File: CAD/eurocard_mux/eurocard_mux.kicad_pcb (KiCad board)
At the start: 2 copper layers, 124 x 60 mm, 20 parts, among them J1 1759091, J2 1759091, J3 MC-254-12-00-RA-DIP, J4 MC-254-12-00-RA-DIP, J5 1759091, K1 AGQ210A12Z, K2 AGQ210A12Z, K3 AGQ210A12Z, K4 AGQ210A12Z, K5 AGQ210A12Z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

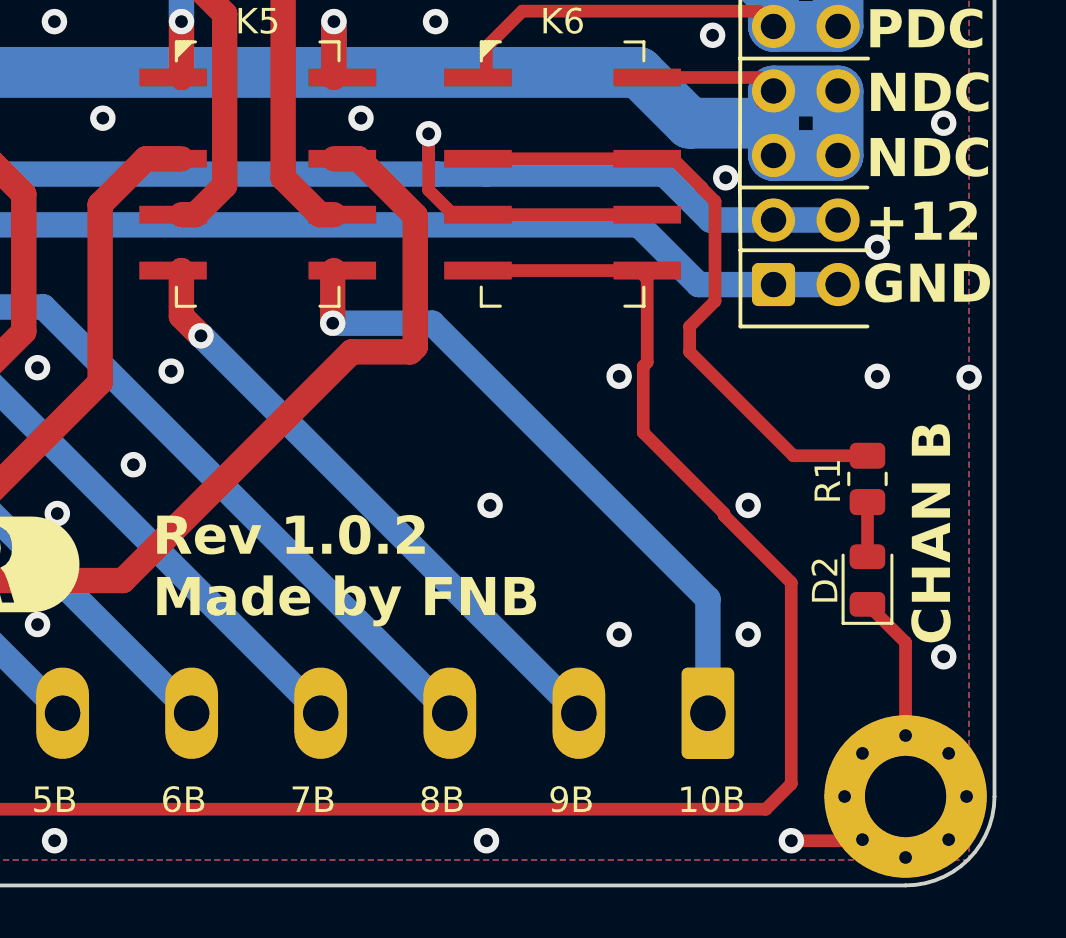
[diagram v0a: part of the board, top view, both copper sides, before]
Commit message: Switched let connections for correct id
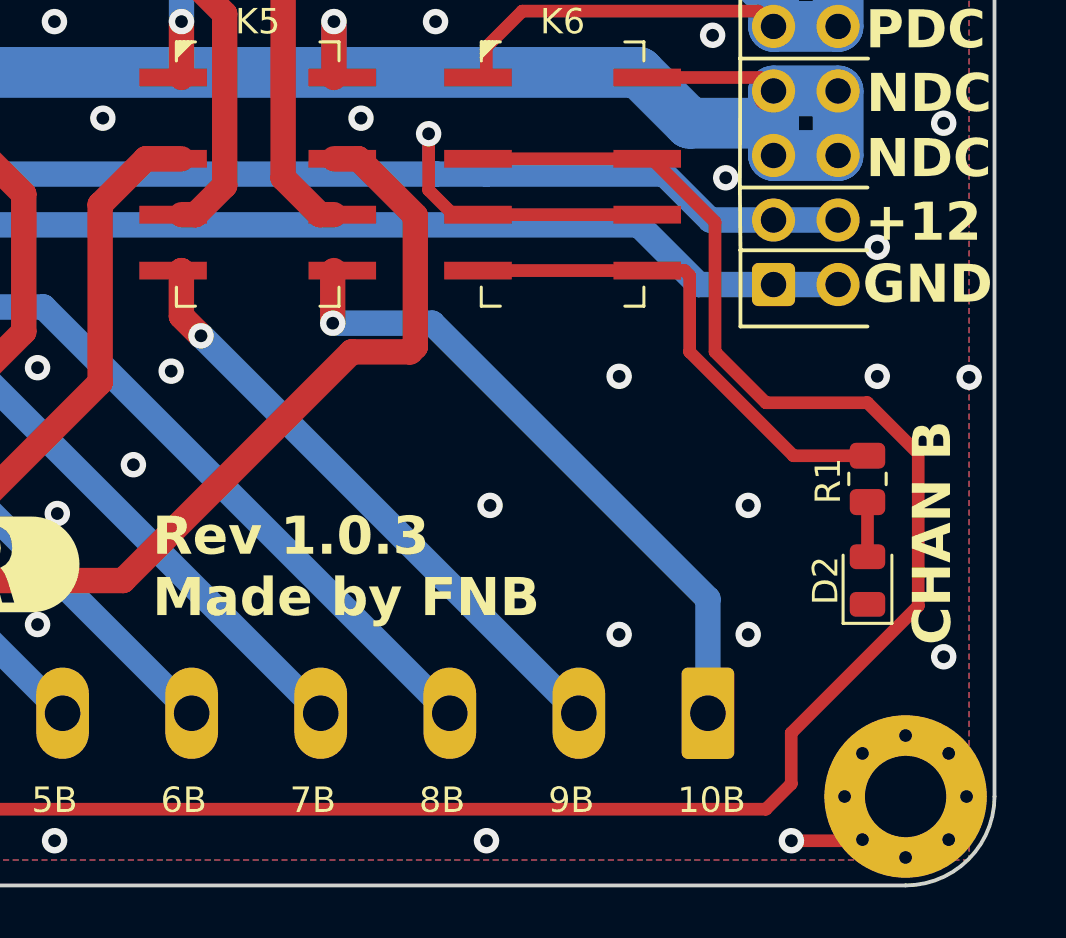
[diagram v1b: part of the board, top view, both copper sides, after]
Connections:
- R1 pad 1: /CHNA -> /CHNB
- R2 pad 1: /CHNB -> /CHNA
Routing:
- net /CHNA: track 24.7 -> 161.7 mm
- net /CHNB: track 150.6 -> 19.8 mm
- net GND: track 161.2 -> 153.0 mm
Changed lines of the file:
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@@
 		(title "Mina ERT multiplexer")
 		(date "2025-12-09")
-		(rev "1.0.2")
+		(rev "1.0.3")
 		(company "Made By FNB")
 	)
@@
 		(property ki_fp_filters "Relay*DPDT*Kemet*EE2*NU*")
 		(sheetname "/")
-		(sheetfile "eurocard mux.kicad_sch")
+		(sheetfile "eurocard_mux.kicad_sch")
 		(attr smd)
 		(fp_line
@@
 		(property ki_fp_filters "Relay*DPDT*Kemet*EE2*NU*")
 		(sheetname "/")
-		(sheetfile "eurocard mux.kicad_sch")
+		(sheetfile "eurocard_mux.kicad_sch")
 		(attr smd)
 		(fp_line
@@
 		(property ki_fp_filters "Relay*DPDT*Kemet*EE2*NU*")
 		(sheetname "/")
-		(sheetfile "eurocard mux.kicad_sch")
+		(sheetfile "eurocard_mux.kicad_sch")
 		(attr smd)
 		(fp_line
@@
 		(property ki_fp_filters "R_*")
 		(sheetname "/")
-		(sheetfile "eurocard mux.kicad_sch")
+		(sheetfile "eurocard_mux.kicad_sch")
 		(attr smd)
 		(fp_line
@@
 			(layers "F.Cu" "F.Mask" "F.Paste")
 			(roundrect_rratio 0.243902)
-			(net 37 "/CHNB")
+			(net 38 "/CHNA")
 			(pintype "passive")
 		)
@@
 		(property ki_fp_filters "Connector*:*_2x??_*")
 		(sheetname "/")
-		(sheetfile "eurocard mux.kicad_sch")
+		(sheetfile "eurocard_mux.kicad_sch")
 		(attr through_hole)
 		(fp_line
@@
 		(property ki_fp_filters "MountingHole*Pad*")
 		(sheetname "/")
-		(sheetfile "eurocard mux.kicad_sch")
+		(sheetfile "eurocard_mux.kicad_sch")
 		(attr exclude_from_pos_files exclude_from_bom)
 		(fp_circle
@@
 		(property ki_fp_filters "LED* LED_SMD:* LED_THT:*")
 		(sheetname "/")
-		(sheetfile "eurocard mux.kicad_sch")
+		(sheetfile "eurocard_mux.kicad_sch")
 		(attr smd)
 		(fp_line
@@
 		(property ki_fp_filters "Relay*DPDT*Kemet*EE2*NU*")
 		(sheetname "/")
-		(sheetfile "eurocard mux.kicad_sch")
+		(sheetfile "eurocard_mux.kicad_sch")
 		(attr smd)
 		(fp_line
@@
 		(property ki_fp_filters "Connector*:*_1x??_*")
 		(sheetname "/")
-		(sheetfile "eurocard mux.kicad_sch")
+		(sheetfile "eurocard_mux.kicad_sch")
 		(attr through_hole)
 		(fp_line
@@
 		(property ki_fp_filters "MountingHole*Pad*")
 		(sheetname "/")
-		(sheetfile "eurocard mux.kicad_sch")
+		(sheetfile "eurocard_mux.kicad_sch")
 		(attr exclude_from_pos_files exclude_from_bom)
 		(fp_circle
@@
 		(property ki_fp_filters "R_*")
 		(sheetname "/")
-		(sheetfile "eurocard mux.kicad_sch")
+		(sheetfile "eurocard_mux.kicad_sch")
 		(attr smd)
 		(fp_line
@@
 			(layers "F.Cu" "F.Mask" "F.Paste")
 			(roundrect_rratio 0.243902)
-			(net 38 "/CHNA")
+			(net 37 "/CHNB")
 			(pintype "passive")
 		)
@@
 		(property ki_fp_filters "MountingHole*Pad*")
 		(sheetname "/")
-		(sheetfile "eurocard mux.kicad_sch")
+		(sheetfile "eurocard_mux.kicad_sch")
 		(attr exclude_from_pos_files exclude_from_bom)
 		(fp_circle
@@
 		(property ki_fp_filters "Relay*DPDT*Kemet*EE2*NU*")
 		(sheetname "/")
-		(sheetfile "eurocard mux.kicad_sch")
+		(sheetfile "eurocard_mux.kicad_sch")
 		(attr smd)
 		(fp_line
@@
 		(property ki_fp_filters "MountingHole*Pad*")
 		(sheetname "/")
-		(sheetfile "eurocard mux.kicad_sch")
+		(sheetfile "eurocard_mux.kicad_sch")
 		(attr exclude_from_pos_files exclude_from_bom)
 		(fp_circle
@@
 		(property ki_fp_filters "LED* LED_SMD:* LED_THT:*")
 		(sheetname "/")
-		(sheetfile "eurocard mux.kicad_sch")
+		(sheetfile "eurocard_mux.kicad_sch")
 		(attr smd)
 		(fp_line
@@
 		(property ki_fp_filters "Relay*DPDT*Kemet*EE2*NU*")
 		(sheetname "/")
-		(sheetfile "eurocard mux.kicad_sch")
+		(sheetfile "eurocard_mux.kicad_sch")
 		(attr smd)
 		(fp_line
@@
 		(property ki_fp_filters "Connector*:*_2x??_*")
 		(sheetname "/")
-		(sheetfile "eurocard mux.kicad_sch")
+		(sheetfile "eurocard_mux.kicad_sch")
 		(attr through_hole)
 		(fp_line
@@
 		(property ki_fp_filters "Connector*:*_1x??_*")
 		(sheetname "/")
-		(sheetfile "eurocard mux.kicad_sch")
+		(sheetfile "eurocard_mux.kicad_sch")
 		(attr through_hole)
 		(fp_line
@@
 		(property ki_fp_filters "Connector*:*_1x??_*")
 		(sheetname "/")
-		(sheetfile "eurocard mux.kicad_sch")
+		(sheetfile "eurocard_mux.kicad_sch")
 		(attr through_hole)
 		(fp_line
@@
 	)
 	(segment
-		(start 175.5 141.5)
-		(end 175.5 135.4375)
-		(width 0.5)
-		(layer "F.Cu")
-		(net 33)
-	)
-	(segment
 		(start 62.5 141.5)
 		(end 64 143)
@@
 	)
 	(segment
-		(start 175.5 135.4375)
-		(end 174 133.9375)
-		(width 0.5)
-		(layer "F.Cu")
-		(net 33)
-	)
-	(segment
 		(start 58.5 88.5)
 		(end 58.5 93.527227)
@@
 	)
 	(segment
-		(start 165.329222 124.415087)
-		(end 165.176477 124.567832)
-		(width 0.5)
-		(layer "F.Cu")
-		(net 37)
-	)
-	(segment
-		(start 165.176477 127.176477)
-		(end 168.354477 130.354477)
-		(width 0.5)
-		(layer "F.Cu")
-		(net 37)
-	)
-	(segment
-		(start 61.85 129.15)
-		(end 63 129.15)
-		(width 0.5)
-		(layer "F.Cu")
-		(net 37)
-	)
-	(segment
-		(start 168.354477 130.435668)
-		(end 171 133.081191)
+		(start 167 121)
+		(end 167 124)
 		(width 0.5)
 		(layer "F.Cu")
@@
 	)
 	(segment
-		(start 171 141)
-		(end 170 142)
+		(start 165 120.8)
+		(end 166.8 120.8)
 		(width 0.5)
 		(layer "F.Cu")
@@
 	)
 	(segment
-		(start 165 120.8)
-		(end 165.329222 121.129222)
+		(start 166.8 120.8)
+		(end 167 121)
 		(width 0.5)
 		(layer "F.Cu")
@@
 	)
 	(segment
-		(start 165.329222 121.129222)
-		(end 165.329222 124.415087)
+		(start 171.0875 128.0875)
+		(end 174 128.0875)
 		(width 0.5)
 		(layer "F.Cu")
@@
 	)
 	(segment
-		(start 165.176477 124.567832)
-		(end 165.176477 127.176477)
+		(start 167 124)
+		(end 171.0875 128.0875)
 		(width 0.5)
 		(layer "F.Cu")
@@
 	)
 	(segment
-		(start 61 137)
-		(end 61 130)
+		(start 174 126)
+		(end 176 128)
 		(width 0.5)
 		(layer "F.Cu")
-		(net 37)
+		(net 38)
 	)
 	(segment
-		(start 66 142)
-		(end 61 137)
+		(start 61 130)
+		(end 61.85 129.15)
 		(width 0.5)
 		(layer "F.Cu")
-		(net 37)
+		(net 38)
 	)
 	(segment
-		(start 168.354477 130.354477)
-		(end 168.354477 130.435668)
+		(start 159 116.4)
+		(end 165 116.4)
 		(width 0.5)
 		(layer "F.Cu")
-		(net 37)
+		(net 38)
 	)
 	(segment
-		(start 61 130)
-		(end 61.85 129.15)
+		(start 168 124)
+		(end 170 126)
 		(width 0.5)
 		(layer "F.Cu")
-		(net 37)
+		(net 38)
 	)
 	(segment
-		(start 170 142)
-		(end 66 142)
+		(start 170 126)
+		(end 174 126)
 		(width 0.5)
 		(layer "F.Cu")
-		(net 37)
+		(net 38)
 	)
 	(segment
-		(start 171 133.081191)
-		(end 171 141)
+		(start 171 141)
+		(end 170 142)
 		(width 0.5)
 		(layer "F.Cu")
-		(net 37)
+		(net 38)
 	)
 	(segment
-		(start 171.0875 128.0875)
-		(end 167 124)
+		(start 176 134)
+		(end 171 139)
 		(width 0.5)
 		(layer "F.Cu")
@@
 	)
 	(segment
-		(start 159 116.4)
-		(end 165 116.4)
+		(start 66 142)
+		(end 61 137)
 		(width 0.5)
 		(layer "F.Cu")
@@
 	)
 	(segment
-		(start 166.349684 116.4)
-		(end 165 116.4)
+		(start 165.511 116.4)
+		(end 168 118.889)
 		(width 0.5)
 		(layer "F.Cu")
@@
 	)
 	(segment
-		(start 167.469104 117.51942)
-		(end 166.349684 116.4)
+		(start 168 118.889)
+		(end 168 124)
 		(width 0.5)
 		(layer "F.Cu")
@@
 	)
 	(segment
-		(start 167 124)
-		(end 167 123)
+		(start 61 137)
+		(end 61 130)
 		(width 0.5)
 		(layer "F.Cu")
@@
 	)
 	(segment
-		(start 174 128.0875)
-		(end 171.0875 128.0875)
+		(start 171 139)
+		(end 171 141)
 		(width 0.5)
 		(layer "F.Cu")
@@
 	)
 	(segment
-		(start 168 122)
-		(end 168 118.072271)
+		(start 61.85 129.15)
+		(end 63 129.15)
 		(width 0.5)
 		(layer "F.Cu")
@@
 	)
 	(segment
-		(start 168 118.072271)
-		(end 167.469104 117.541375)
+		(start 170 142)
+		(end 66 142)
 		(width 0.5)
 		(layer "F.Cu")
@@
 	)
 	(segment
-		(start 167 123)
-		(end 168 122)
+		(start 176 128)
+		(end 176 134)
 		(width 0.5)
 		(layer "F.Cu")
@@
 	)
 	(segment
-		(start 167.469104 117.541375)
-		(end 167.469104 117.51942)
+		(start 165 116.4)
+		(end 165.511 116.4)
 		(width 0.5)
 		(layer "F.Cu")
